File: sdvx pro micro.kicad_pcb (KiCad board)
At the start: 2 copper layers, 124 x 44 mm, 15 parts

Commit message: button layout done
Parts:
- removed BT-A, BT-B, BT-C, BT-D, FX-L, FX-R, START: JST_XH_B4B-XH-A_1x04_P2.50mm_Vertical, Connector_JST:JST_XH_B4B-XH-A_1x04_P2.50mm_Vertical
- removed Pot L: JST_PH_B3B-PH-K_1x03_P2.00mm_Vertical, Connector_JST:JST_PH_B3B-PH-K_1x03_P2.00mm_Vertical
- removed Pot R: JST_PH_B3B-PH-K_1x03_P2.00mm_Vertical, Connector_JST:JST_PH_B3B-PH-K_1x03_P2.00mm_Vertical
- removed the REF** at (35.0, 4.00)
- removed the REF** at (34.8, 24.8)
- added A1: RaspberryPi_Pico, Module:RaspberryPi_Pico_Common_Unspecified, F.Cu at (152.1, 94.0)
- added C1: C_Small, Capacitor_THT:C_Disc_D4.3mm_W1.9mm_P5.00mm, F.Cu at (127.1, 80.9)
- added J1: BT A, Connector_JST:JST_XH_B4B-XH-A_1x04_P2.50mm_Vertical, F.Cu at (105.4, 111.3)
- added J10: ENC L, Connector_JST:JST_XH_B4B-XH-A_1x04_P2.50mm_Vertical, F.Cu at (135.3, 75.6)
- added J11: ENC R, Connector_JST:JST_XH_B4B-XH-A_1x04_P2.50mm_Vertical, F.Cu at (164.0, 75.3)
- added J2: BT B, Connector_JST:JST_XH_B4B-XH-A_1x04_P2.50mm_Vertical, F.Cu at (134.3, 111.3)
- added J3: BT C, Connector_JST:JST_XH_B4B-XH-A_1x04_P2.50mm_Vertical, F.Cu at (163.2, 111.3)
- added J4: BT D, Connector_JST:JST_XH_B4B-XH-A_1x04_P2.50mm_Vertical, F.Cu at (192.0, 111.3)
- added J5: FX L, Connector_JST:JST_XH_B4B-XH-A_1x04_P2.50mm_Vertical, F.Cu at (119.9, 111.3)
- added J6: FX R, Connector_JST:JST_XH_B4B-XH-A_1x04_P2.50mm_Vertical, F.Cu at (177.6, 111.3)
- added J7: Start, Connector_JST:JST_XH_B4B-XH-A_1x04_P2.50mm_Vertical, F.Cu at (148.7, 111.3)
- added J8: POT L, Connector_JST:JST_PH_B3B-PH-K_1x03_P2.00mm_Vertical, F.Cu at (126.8, 76.4)
- added J9: POT R, Connector_JST:JST_PH_B3B-PH-K_1x03_P2.00mm_Vertical, F.Cu at (178.2, 75.2)
- added Q1: BSS138, Package_TO_SOT_SMD:SOT-23, F.Cu at (111.4, 105.5)
- added Q2: BSS138, Package_TO_SOT_SMD:SOT-23, F.Cu at (118.7, 105.5)
- added Q3: BSS138, Package_TO_SOT_SMD:SOT-23, F.Cu at (185.4, 106.5)
- added Q4: BSS138, Package_TO_SOT_SMD:SOT-23, F.Cu at (193.4, 106.5)
- added Q5: BSS138, Package_TO_SOT_SMD:SOT-23, F.Cu at (115.0, 105.5)
- added Q6: BSS138, Package_TO_SOT_SMD:SOT-23, F.Cu at (189.4, 106.5)
- added Q7: BSS138, Package_TO_SOT_SMD:SOT-23, F.Cu at (122.3, 105.5)
- added R1: 1k, Resistor_THT:R_Axial_DIN0204_L3.6mm_D1.6mm_P7.62mm_Horizontal, F.Cu at (117.3, 79.9)
- added R2: 2k, Resistor_THT:R_Axial_DIN0204_L3.6mm_D1.6mm_P7.62mm_Horizontal, F.Cu at (114.1, 79.9)
- added R3: 1k, Resistor_THT:R_Axial_DIN0204_L3.6mm_D1.6mm_P7.62mm_Horizontal, F.Cu at (196.3, 80.8)
- added R4: 2k, Resistor_THT:R_Axial_DIN0204_L3.6mm_D1.6mm_P7.62mm_Horizontal, F.Cu at (193.2, 80.8)
- added SW1: SW_DIP_x01, Button_Switch_SMD:SW_DIP_SPSTx01_Slide_9.78x4.72mm_W8.61mm_P2.54mm, F.Cu at (153.9, 75.7)
- moved REF** 124.1 mm to (96.5, 78.0)
- moved REF** 124.1 mm to (208.5, 78.0)
- moved REF** 124.1 mm to (96.5, 110.0)
- moved REF** 124.1 mm to (208.5, 110.0)
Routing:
- net 5V: track 243.9 -> 0.00 mm
- net Ground: track 227.3 -> 0.00 mm
- net ButtonData: track 211.9 -> 0.00 mm, vias 1 -> 0
- net LightData: track 210.9 -> 0.00 mm, vias 2 -> 0
- net GND: track 0.00 -> 118.9 mm
- net EncData: track 104.7 -> 0.00 mm
- net +5V: track 0.00 -> 81.0 mm
- net Net-(A1-GPIO10): track 0.00 -> 51.3 mm
- net Net-(A1-GPIO6): track 0.00 -> 47.2 mm
- net Net-(A1-GPIO9): track 0.00 -> 42.3 mm
- net Net-(A1-GPIO5): track 0.00 -> 37.8 mm
- net Net-(A1-GPIO11): track 0.00 -> 37.0 mm
- net Net-(A1-GPIO8): track 0.00 -> 36.1 mm
- net START LED: track 0.00 -> 32.6 mm
- net Net-(A1-GPIO7): track 0.00 -> 29.6 mm
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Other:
- board text removed: "5V"
- board text removed: "BTN"
- board text removed: "GND"
- board text removed: "JST-PH 3 Pin"
- board text removed: "JST-XH 4 Pin"
- board text removed: "LED"
- board text removed: "M5 Screws"
- board text removed: "Minnowboard V3"
- board text removed: "Out"
- board text removed: "Pi Pico"

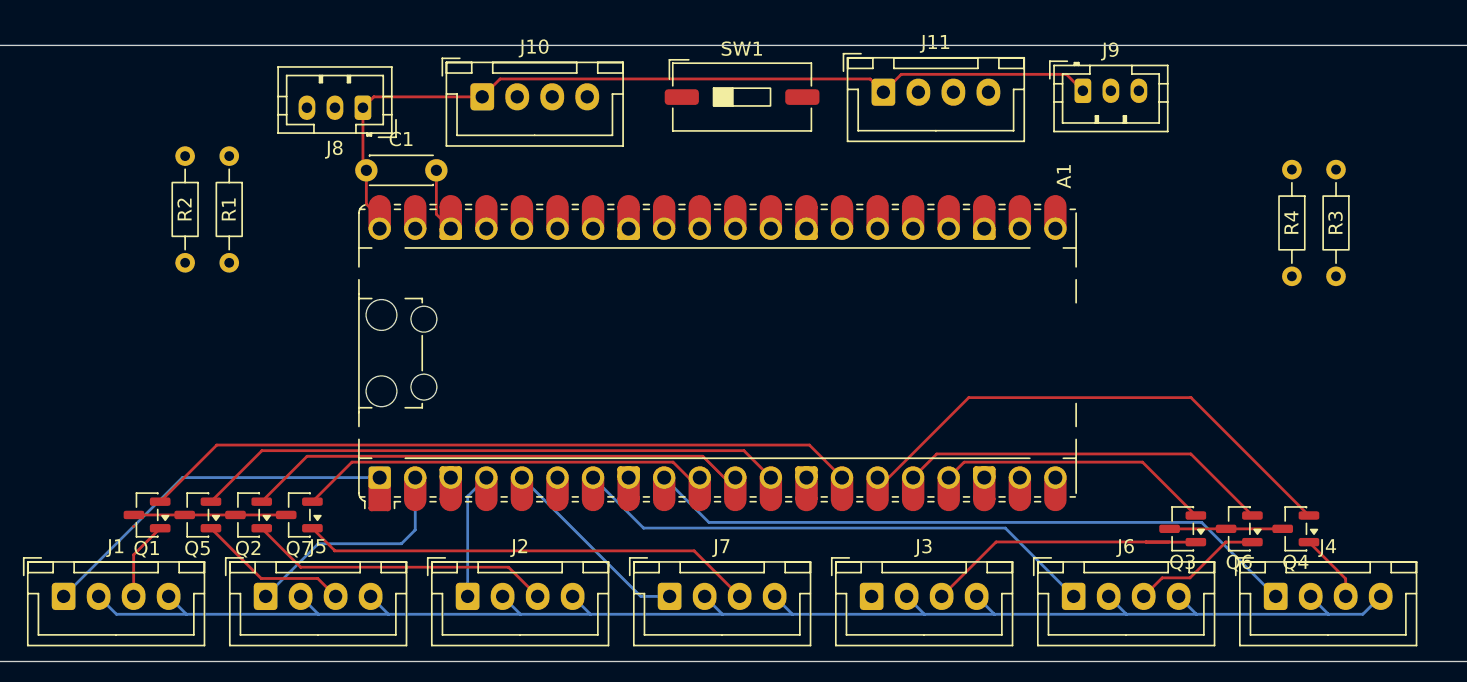
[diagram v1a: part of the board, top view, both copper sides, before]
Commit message: fix wiring issues, add pictures
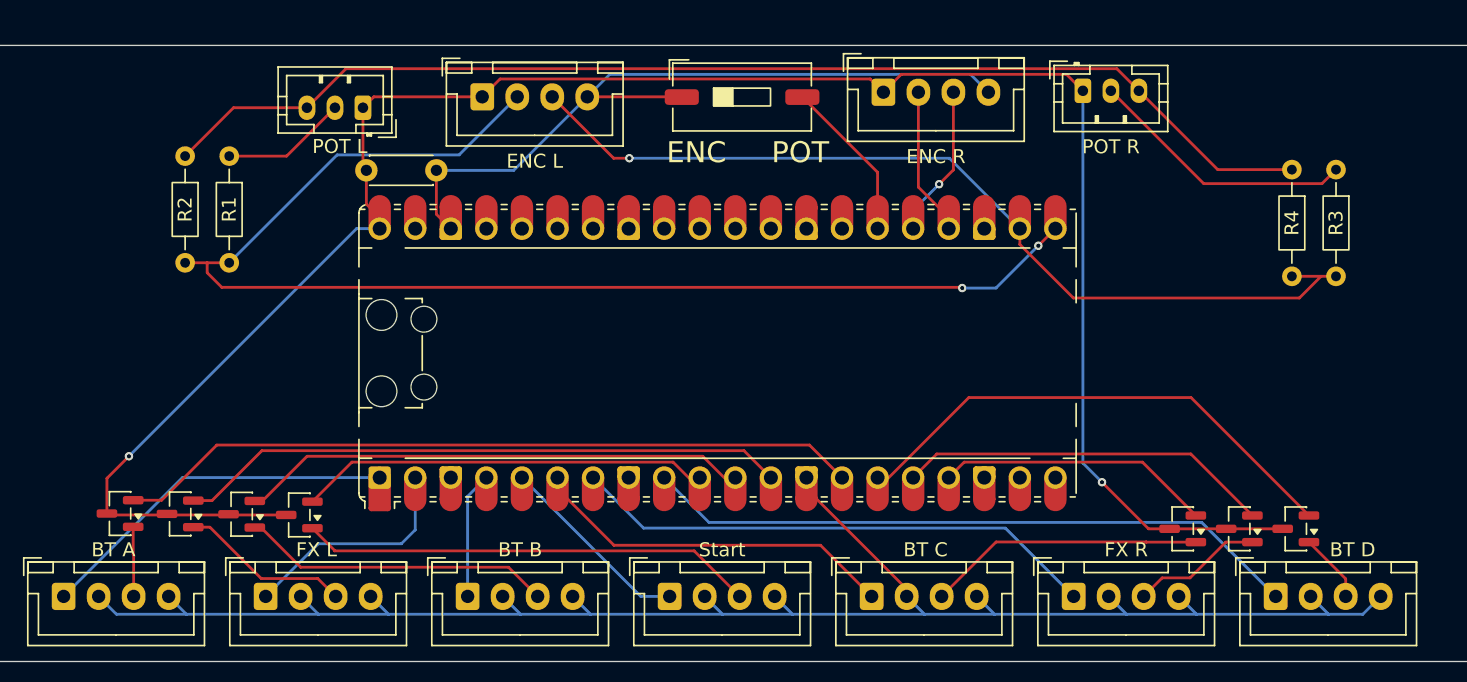
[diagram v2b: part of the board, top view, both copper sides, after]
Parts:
- moved Q1 1.93 mm to (109.5, 105.4)
- moved Q5 1.26 mm to (113.8, 105.4)
- moved Q2 0.49 mm to (118.2, 105.5)
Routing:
- net Net-(A1-GPIO16): track 0.00 -> 92.1 mm, vias 0 -> 2
- net AGND: track 0.00 -> 84.6 mm
- net +5V: track 81.0 -> 147.0 mm, vias 0 -> 2
- net Net-(A1-GPIO17): track 0.00 -> 65.3 mm, vias 0 -> 1
- net GND: track 118.9 -> 179.1 mm
- net Net-(A1-GPIO4): track 0.00 -> 25.6 mm
- net Net-(J9-Pin_2): track 0.00 -> 19.2 mm
- net Net-(A1-GPIO19): track 0.00 -> 10.9 mm, vias 0 -> 1
- net Net-(A1-GPIO20): track 0.00 -> 10.8 mm
- net Net-(A1-GPIO18): track 0.00 -> 9.84 mm
- net Net-(J8-Pin_2): track 0.00 -> 8.98 mm
- net Net-(A1-GPIO10): track 51.3 -> 53.2 mm
- net BT-C LED: track 21.4 -> 19.8 mm
- net FX-L LED: track 10.9 -> 12.2 mm
- net Net-(A1-GPIO9): track 42.3 -> 43.5 mm
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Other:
- board text added: "1k"
- board text added: "2k"
- board text added: "5V"
- board text added: "A"
- board text added: "B"
- board text added: "BTN"
- board text added: "ENC"
- board text added: "GND"
- board text added: "LED"
- board text added: "M5 Screw"
- board text added: "Minnowboard V3"
- board text added: "OUT"
- board text added: "POT"
- board text added: "github.com/minnowfeather/minnowboard"
